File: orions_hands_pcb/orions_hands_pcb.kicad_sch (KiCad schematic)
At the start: 2 parts, among them P1 USB_C_Plug_USB2.0, U2 USBLC6-2SC6

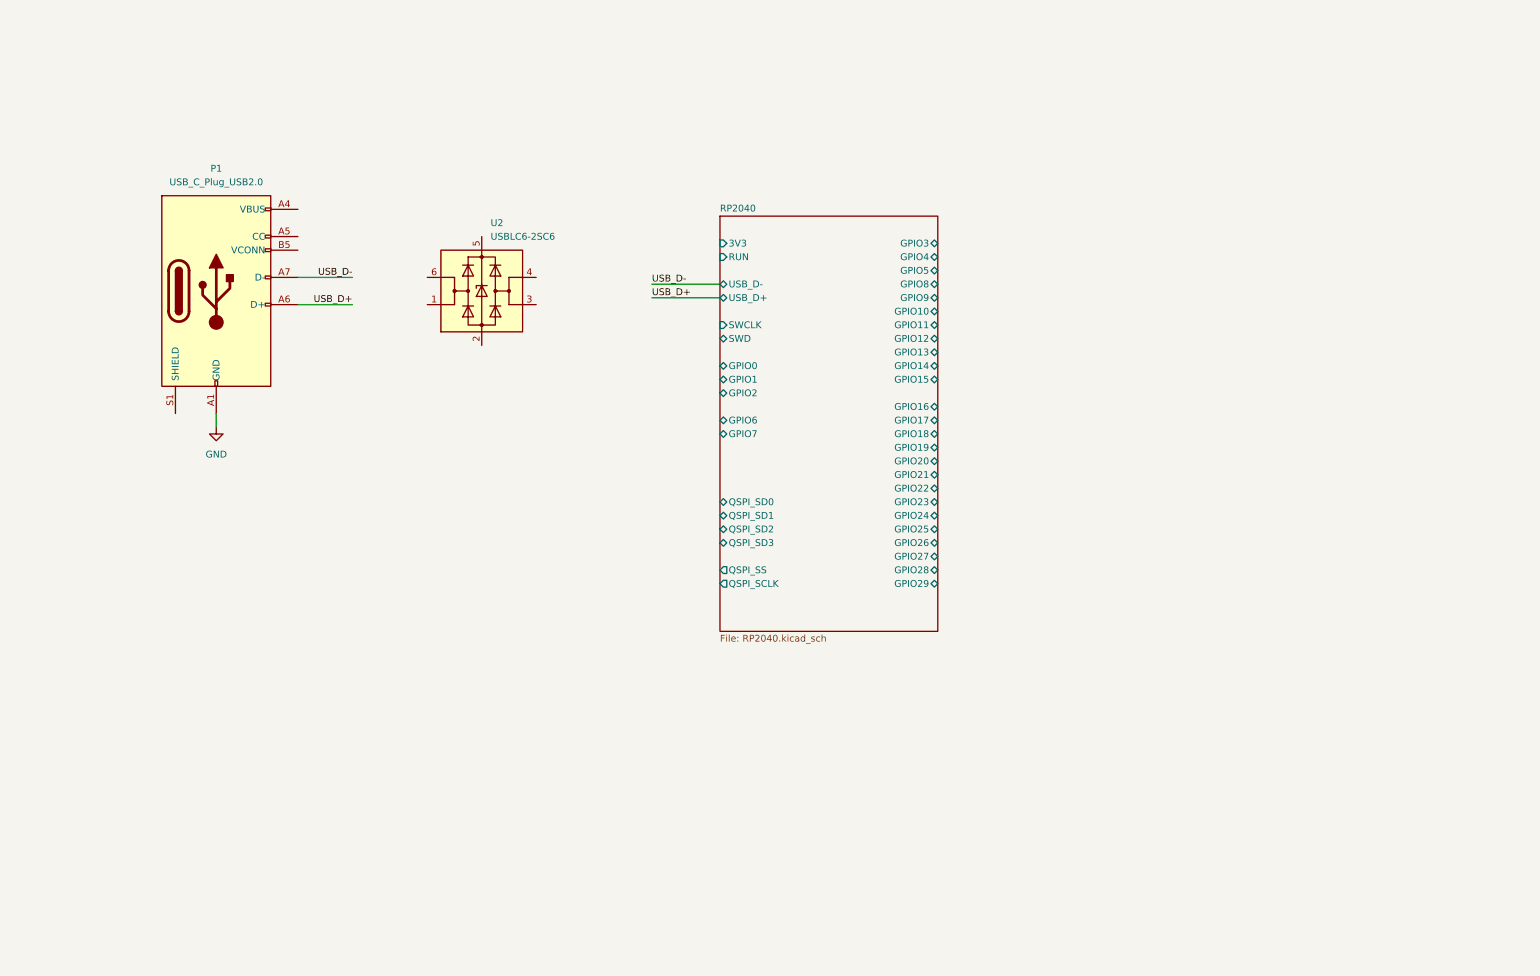
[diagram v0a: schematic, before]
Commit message: usbc, buttons, leds, flash added
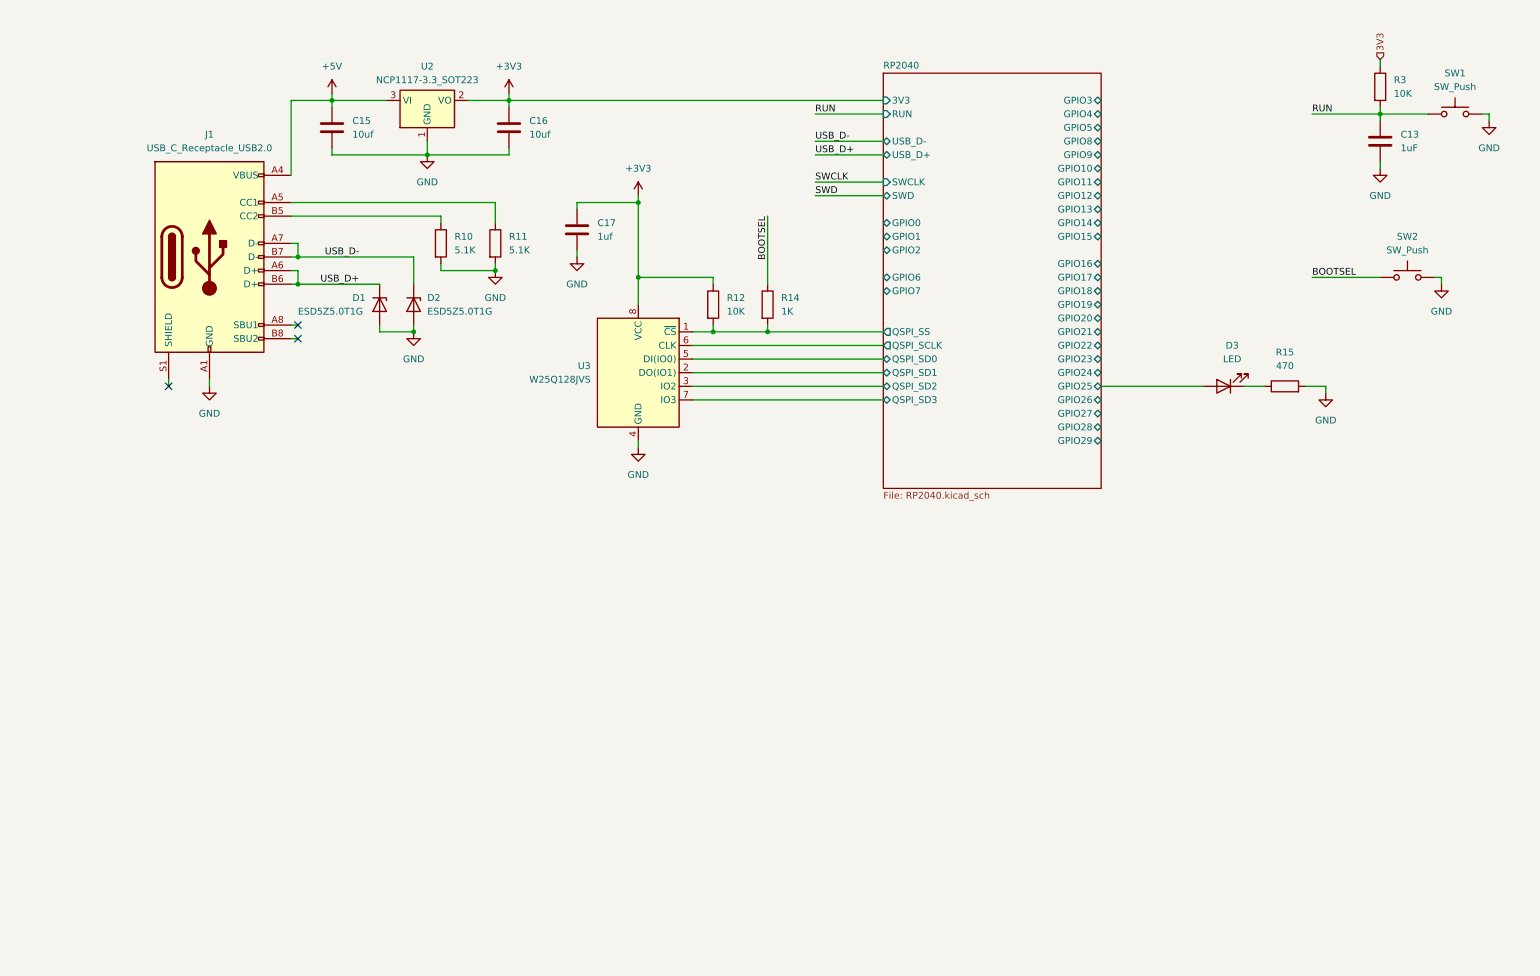
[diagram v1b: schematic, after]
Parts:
- removed P1: USB_C_Plug_USB2.0, symbol Connector:USB_C_Plug_USB2.0
- removed U2: USBLC6-2SC6, Package_TO_SOT_SMD:SOT-23-6, symbol Power_Protection:USBLC6-2SC6
- added C13: 1uF, symbol Device:C
- added C15, C16: 10uf, symbol Device:C
- added C17: 1uf, symbol Device:C
- added D1, D2: ESD5Z5.0T1G, Diode_SMD:D_SOD-523, symbol Diode:ESD5Zxx
- added D3: LED, symbol Device:LED
- added J1: USB_C_Receptacle_USB2.0, symbol Connector:USB_C_Receptacle_USB2.0
- added R10, R11: 5.1K, symbol Device:R
- added R12, R3: 10K, symbol Device:R
- added R14: 1K, symbol Device:R
- added R15: 470, symbol Device:R
- added SW1, SW2: SW_Push, symbol Switch:SW_Push
- added U2: NCP1117-3.3_SOT223, Package_TO_SOT_SMD:SOT-223-3_TabPin2, symbol Regulator_Linear:NCP1117-3.3_SOT223
- added U3: W25Q128JVS, Package_SO:SOIC-8_5.23x5.23mm_P1.27mm, symbol Memory_Flash:W25Q128JVS
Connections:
- net GND: now also C13.2, C15.2, C16.2, C17.2, D1.2 (A), D2.2 (A), J1.A1 (GND), J1.A12 (GND), J1.B1 (GND), J1.B12 (GND), R10.2, R11.2, R15.2, SW1.2, SW2.2, U2.1 (GND), U3.4 (GND)
- net RP2040/GPIO25: now also D3.2 (A)
- net RP2040/QSPI_SCLK: now also U3.6 (CLK)
- net RP2040/QSPI_SD0: now also U3.5 (DI(IO0))
- net RP2040/QSPI_SD1: now also U3.2 (DO(IO1))
- net RP2040/QSPI_SD2: now also U3.3 (IO2)
- net RP2040/QSPI_SD3: now also U3.7 (IO3)
- net RP2040/QSPI_SS: now also R12.2, R14.2, U3.1 (~{CS})
- net USB_D+: now also D1.1 (K), J1.A6 (D+), J1.B6 (D+)
- net USB_D-: now also D2.1 (K), J1.A7 (D-), J1.B7 (D-)
- new net: D3.1 (K), R15.1
- new net: J1.B5 (CC2), R10.1
- new net: J1.A5 (CC1), R11.1
- new net +3V3: C16.1, C17.1, R12.1, U2.2 (VO), U3.8 (VCC)
- new net +5V: C15.1, J1.A4 (VBUS), J1.A9 (VBUS), J1.B4 (VBUS), J1.B9 (VBUS), U2.3 (VI)
- new net 3V3: R3.1
- new net BOOTSEL: R14.1, SW2.1
- new net RUN: C13.1, R3.2, SW1.1
- no-connect marks 0 -> 3

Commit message: added power management + refined
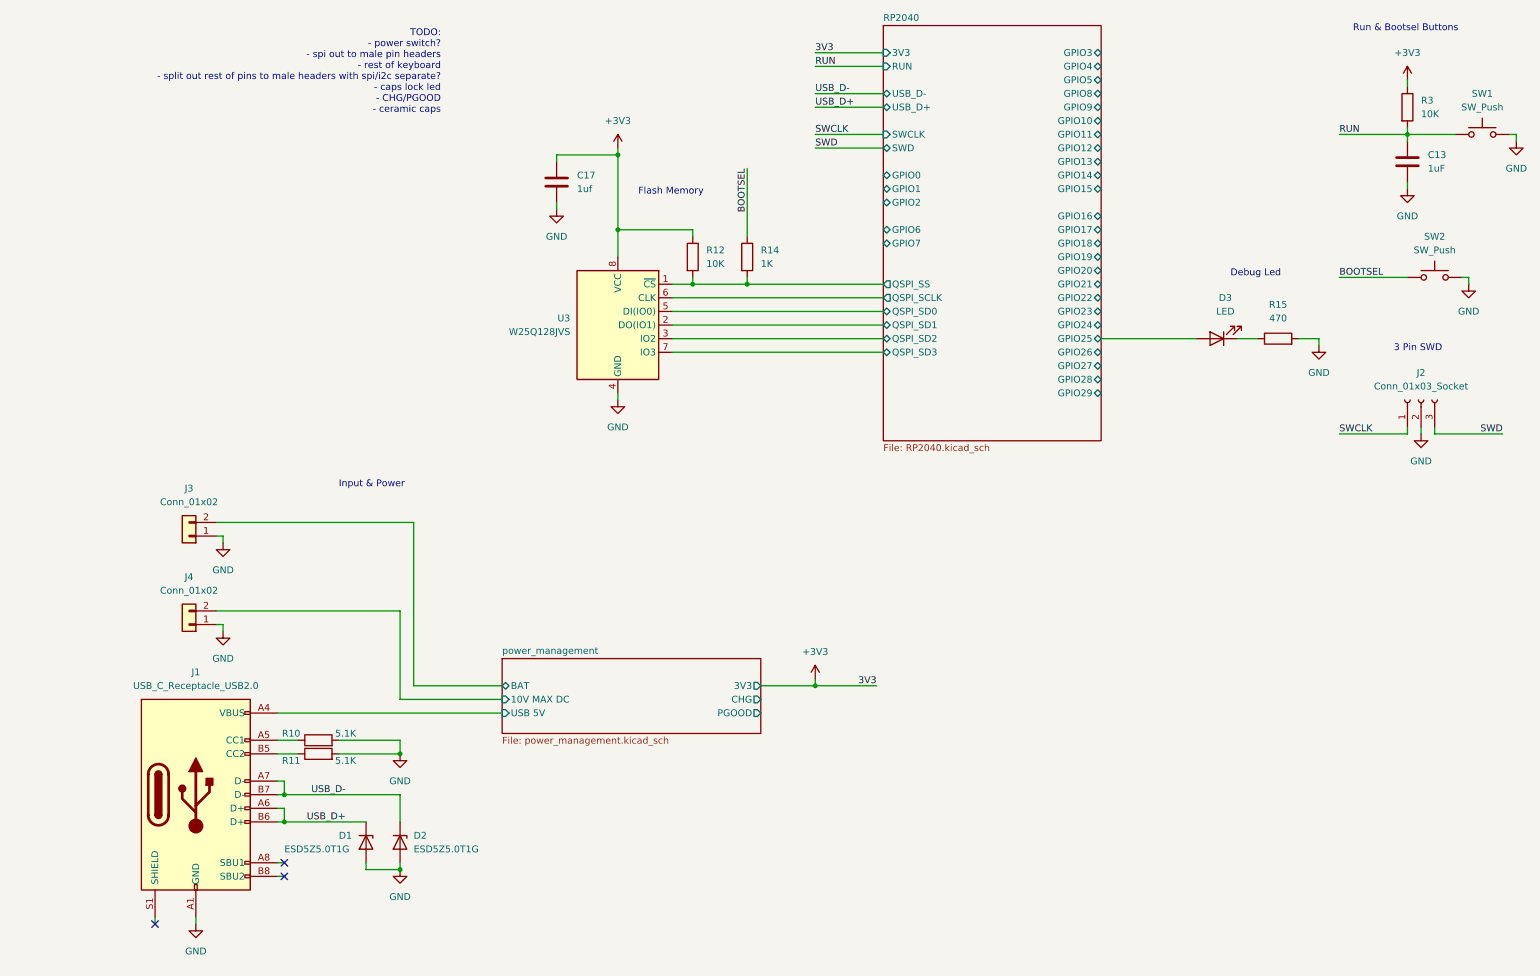
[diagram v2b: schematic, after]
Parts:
- removed C15, C16: 10uf, symbol Device:C
- removed U2: NCP1117-3.3_SOT223, Package_TO_SOT_SMD:SOT-223-3_TabPin2, symbol Regulator_Linear:NCP1117-3.3_SOT223
- added J2: Conn_01x03_Socket, symbol Connector:Conn_01x03_Socket
- added J3, J4: Conn_01x02, symbol Connector_Generic:Conn_01x02
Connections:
- net 3V3 is gone; now on net +3V3: R3.1
- net GND: now also J2.2 (Pin_2), J3.1 (Pin_1), J4.1 (Pin_1)
- net SWCLK: now also J2.1 (Pin_1)
- net SWD: now also J2.3 (Pin_3)
- net at R10.1: now also J1.A5 (CC1); no longer J1.B5 (CC2)
- net at R11.1: now also J1.B5 (CC2); no longer J1.A5 (CC1)
- net +5V renamed power_management/USB 5V
- new net power_management/10V MAX DC: J4.2 (Pin_2)
- new net power_management/BAT: J3.2 (Pin_2)
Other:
- added sheet power_management (power_management.kicad_sch)
- note added: "3 Pin SWD"
- note added: "Debug Led"
- note added: "Flash Memory"
- note added: "Input & Power"
- note added: "Run & Bootsel Buttons"
- note added: "TODO: - power switch? - spi out to male pin headers - rest of keyboard - split out rest of pins to male headers with spi/i2c separate? - caps lock led - CHG/PGOOD - ceramic caps"
- moved on the sheet: C13, C17, D3, R12, R14, R15, R3, SW1, SW2, U3

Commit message: added items for todo
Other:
- note added: "TODO: - power switch? - spi out to male pin headers for display / think about Chip Select can make this more effective with 2 spi headers using same pins - rest of keyboard (pull up resistors + split space) - split out rest of pins to male headers with spi/i2c separate? so can add dw1000? or UART? - caps lock led - CHG/PGOOD - ceramic caps"
- note removed: "TODO: - power switch? - spi out to male pin headers - rest of keyboard - split out rest of pins to male headers with spi/i2c separate? - caps lock led - CHG/PGOOD - ceramic caps"
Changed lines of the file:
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@@
     (effects (font (size 1.27 1.27)) (justify left bottom))
   )
-  (text "TODO: \n- power switch?\n- spi out to male pin headers\n- rest of keyboard\n- split out rest of pins to male headers with spi/i2c separate?\n- caps lock led\n- CHG/PGOOD\n- ceramic caps"
-    (at 78.74 34.29 0)
+  (text "TODO: \n- power switch?\n- spi out to male pin headers\n	for display / think about Chip Select \n	can make this more effective with 2 spi headers using same pins\n- rest of keyboard (pull up resistors + split space)\n- split out rest of pins to male headers with spi/i2c separate?\n	so can add dw1000? or UART?\n- caps lock led\n- CHG/PGOOD\n- ceramic caps"
+    (at 80.01 38.1 0)
     (effects (font (size 1.27 1.27) (color 255 134 20 1)) (justify right bottom))
   )

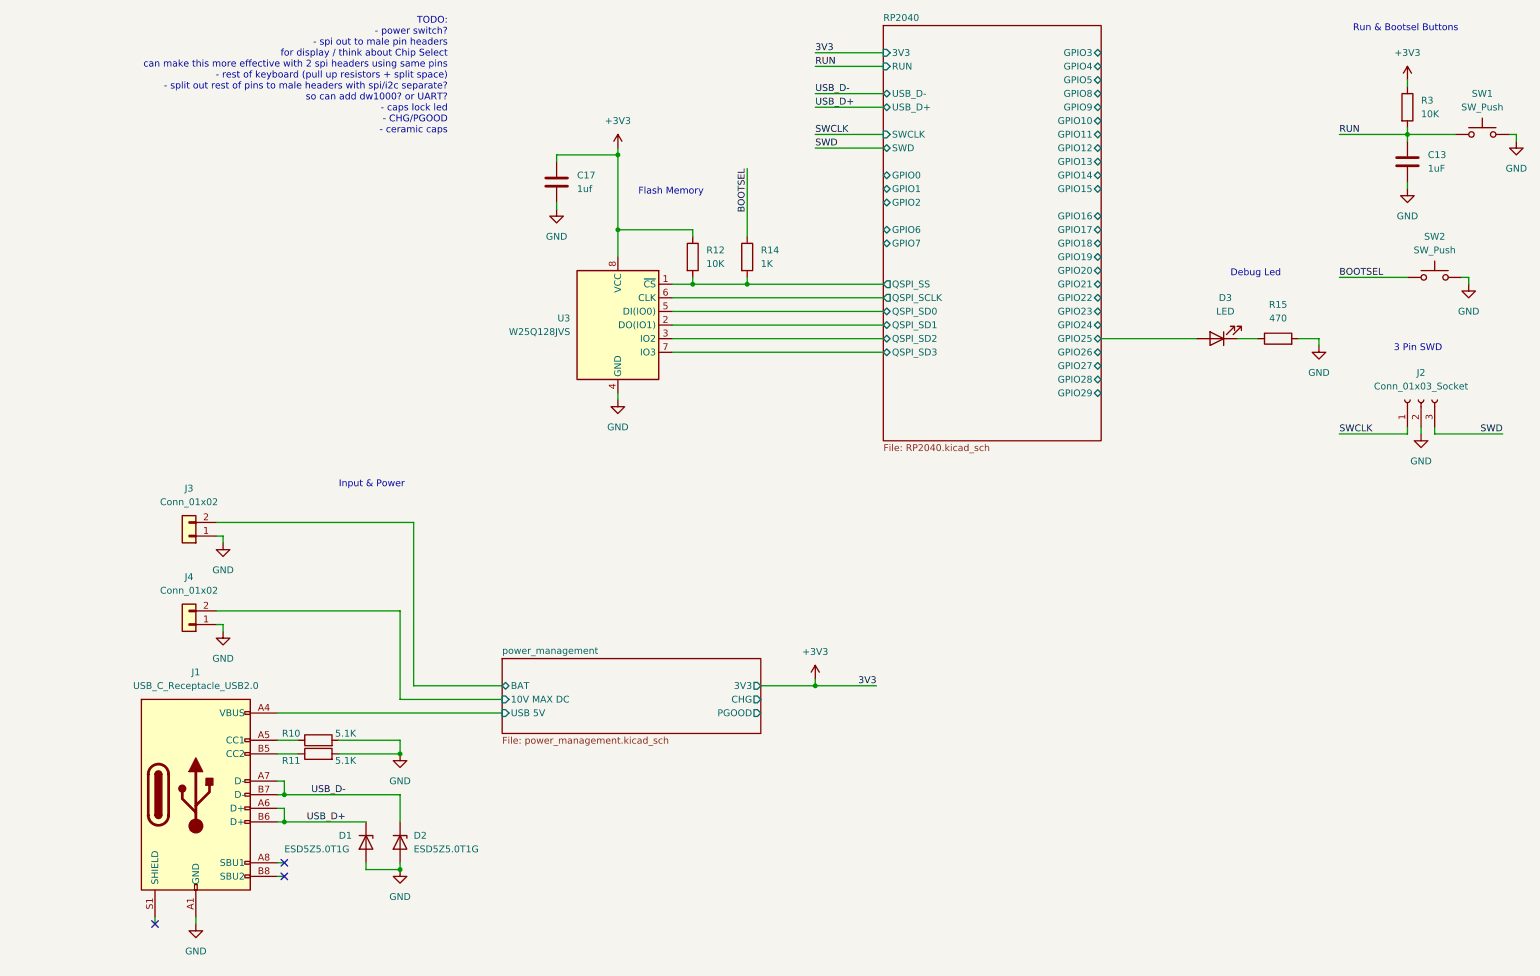
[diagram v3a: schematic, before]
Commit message: SPI pin additions + gpio labeling
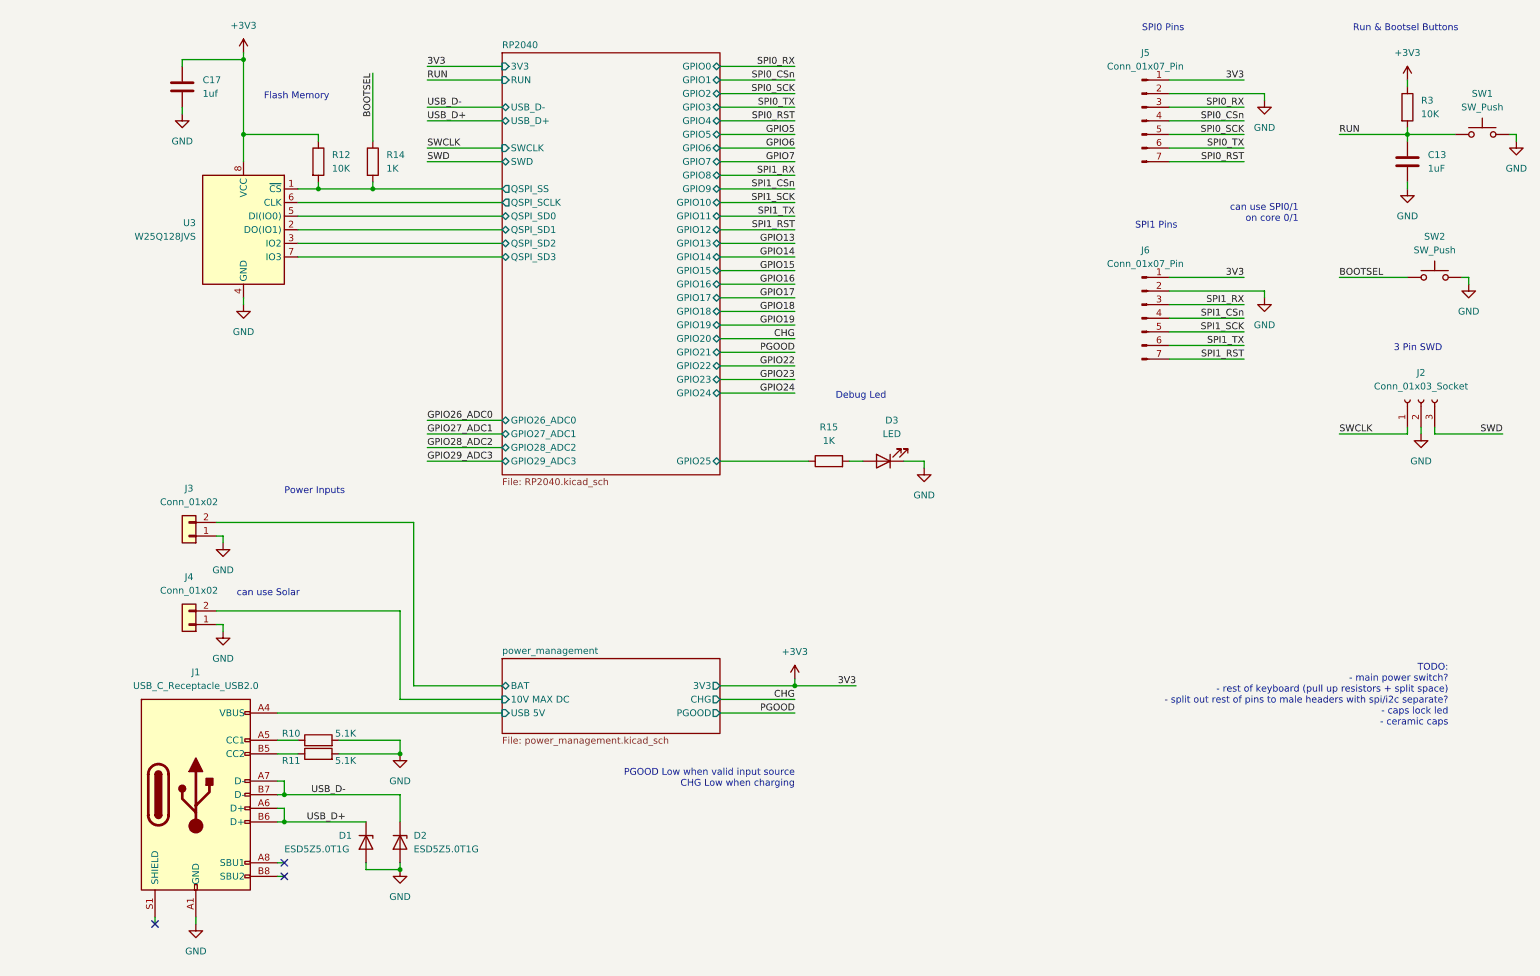
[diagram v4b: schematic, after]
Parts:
- added J5, J6: Conn_01x07_Pin, symbol Connector:Conn_01x07_Pin
- R15: value 470 -> 1K
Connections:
- net +3V3: now also J5.1 (Pin_1), J6.1 (Pin_1)
- net GND: now also D3.1 (K), J5.2 (Pin_2), J6.2 (Pin_2); no longer R15.2
- net RP2040/GPIO25: now also R15.1; no longer D3.2 (A)
- new net: D3.2 (A), R15.2
- new net SPI0_CSn: J5.4 (Pin_4)
- new net SPI0_RST: J5.7 (Pin_7)
- new net SPI0_RX: J5.3 (Pin_3)
- new net SPI0_SCK: J5.5 (Pin_5)
- new net SPI0_TX: J5.6 (Pin_6)
- new net SPI1_CSn: J6.4 (Pin_4)
- new net SPI1_RST: J6.7 (Pin_7)
- new net SPI1_RX: J6.3 (Pin_3)
- new net SPI1_SCK: J6.5 (Pin_5)
- new net SPI1_TX: J6.6 (Pin_6)
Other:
- sheet RP2040 ports: added GPIO26_ADC0, GPIO27_ADC1, GPIO28_ADC2, GPIO29_ADC3; removed GPIO26, GPIO27, GPIO28, GPIO29
- note added: "PGOOD Low when valid input source CHG Low when charging"
- note added: "Power Inputs"
- note added: "SPI0 Pins"
- note added: "SPI1 Pins"
- note added: "TODO: - main power switch? - rest of keyboard (pull up resistors + split space) - split out rest of pins to male headers with spi/i2c separate? - caps lock led - ceramic caps"
- note added: "can use SPI0/1 on core 0/1"
- note added: "can use Solar"
- note removed: "Input & Power"
- note removed: "TODO: - power switch? - spi out to male pin headers for display / think about Chip Select can make this more effective with 2 spi headers using same pins - rest of keyboard (pull up resistors + split space) - split out rest of pins to male headers with spi/i2c separate? so can add dw1000? or UART? - caps lock led - CHG/PGOOD - ceramic caps"
- moved on the sheet: C17, D3, R12, R14, U3

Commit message: Update orions_hands_pcb.kicad_sch
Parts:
- removed D1, D2: ESD5Z5.0T1G, Diode_SMD:D_SOD-523, symbol Diode:ESD5Zxx
- added U2: USBLC6-2SC6, Package_TO_SOT_SMD:SOT-23-6, symbol Power_Protection:USBLC6-2SC6
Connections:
- net GND: now also J1.S1 (SHIELD), U2.2 (GND)
- net USB_D+: now also U2.4 (I/O2); no longer J1.A6 (D+), J1.B6 (D+)
- net USB_D-: now also U2.6 (I/O1); no longer J1.A7 (D-), J1.B7 (D-)
- net power_management/USB 5V: now also U2.5 (VBUS)
- new net: J1.A6 (D+), J1.B6 (D+), U2.3 (I/O2)
- new net: J1.A7 (D-), J1.B7 (D-), U2.1 (I/O1)
- no-connect marks 3 -> 2
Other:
- note added: "add SR1020? embbed or separate modules"

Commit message: typo correction
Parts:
- renumbered C13 to C18, R3 to R13
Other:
- note added: "add SR1020? embed or separate modules"
- note removed: "add SR1020? embbed or separate modules"
